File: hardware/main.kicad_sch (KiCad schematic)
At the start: 430 parts, among them J1 DS1128-09-S8B8X, J10 AS0BC21-S30BM-7H, J2 DS1128-09-S8B8X, J3 DS1128-09-S8B8X, J4 98424-G52-04ALF, J5 miniPCI-E_52P_5.2, J8 USB_C_Receptacle, J9 TYPE-C-31-M-12, Q1 SSM6J501NU, Q3 FDV301N, SW1 TS-1187A-B-A-B, SW2 TS-1187A-B-A-B, U1 SSD1306-OLED-0.91, U10 W25Q256FVEIG, U12 TPD2EUSB30, U13 TPD2EUSB30, U14 TPD2EUSB30, U15 IP5328P, U2 MT7621A, U3 TPS63020, U4 TPS63020, U5 MT3420B, U6 MT3420B, U7 MT3420B, U8 MT3420B, U9 NT5CB64M16FP-DH (!), Y1 X322540MPB4SI

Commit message: update pcb
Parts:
- removed C34: 100u, Capacitor_Tantalum_SMD:CP_EIA-7343-31_Kemet-D, symbol Device:C_Polarized_Small
- removed JP5, JP6: JP, MAS_Package_nostd:SolderJumper_Open_Pad0.5x0.8mm, symbol Jumper:Jumper_2_Open
- added C143, C34: 47u, Capacitor_SMD:C_0805_2012Metric, symbol Device:C_Small
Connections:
- net +1V0: now also C30.1, C41.1, C44.1, L5.2, R30.2; no longer C102.1, C104.1, C106.1, C109.1, C110.1, C115.1, C12.1, C135.1, C136.1, C8.1, C87.1, C93.1, L8.2, U2.N10 (DVDD_K_1), U2.N6 (AVDD10_AFE_P0), U2.N8 (AVDD10_AFE_P2), U2.P10 (DVDD_K_1), U2.P6 (AVDD10_AFE_P1), U2.P8 (AVDD10_AFE_P3), U2.R10 (DVDD_K_1), U2.R6 (AVDD10), U2.R8 (AVDD10_AFE_P4), U2.T10 (DVDD_K_1)
- net +1V2: now also C125.1, C51.1, C53.1, L6.2, R36.2
- net +5V: now also C143.1, C34.1
- net -BATT: now also C143.2, C34.2
- new net +1V0E: C102.1, C104.1, C106.1, C109.1, C110.1, C115.1, C12.1, C135.1, C136.1, C8.1, C87.1, C93.1, L8.2, U2.N10 (DVDD_K_1), U2.N6 (AVDD10_AFE_P0), U2.N8 (AVDD10_AFE_P2), U2.P10 (DVDD_K_1), U2.P6 (AVDD10_AFE_P1), U2.P8 (AVDD10_AFE_P3), U2.R10 (DVDD_K_1), U2.R6 (AVDD10), U2.R8 (AVDD10_AFE_P4), U2.T10 (DVDD_K_1)
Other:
- note added: "DDR3"
- note added: "Ethernet"
- note added: "Interface unit"
- note added: "M.2 connector"
- note added: "OLED"
- note added: "Power bank"
- note added: "Primary power"
- note added: "SPI Flash"
- note added: "SYS"
- note added: "Secondary power"
- note added: "USB3"
- note added: "mPCIe connector"
- moved on the sheet: C1, C10, C100, C101, C102, C103, C104, C105, C106, C107, C108, C109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

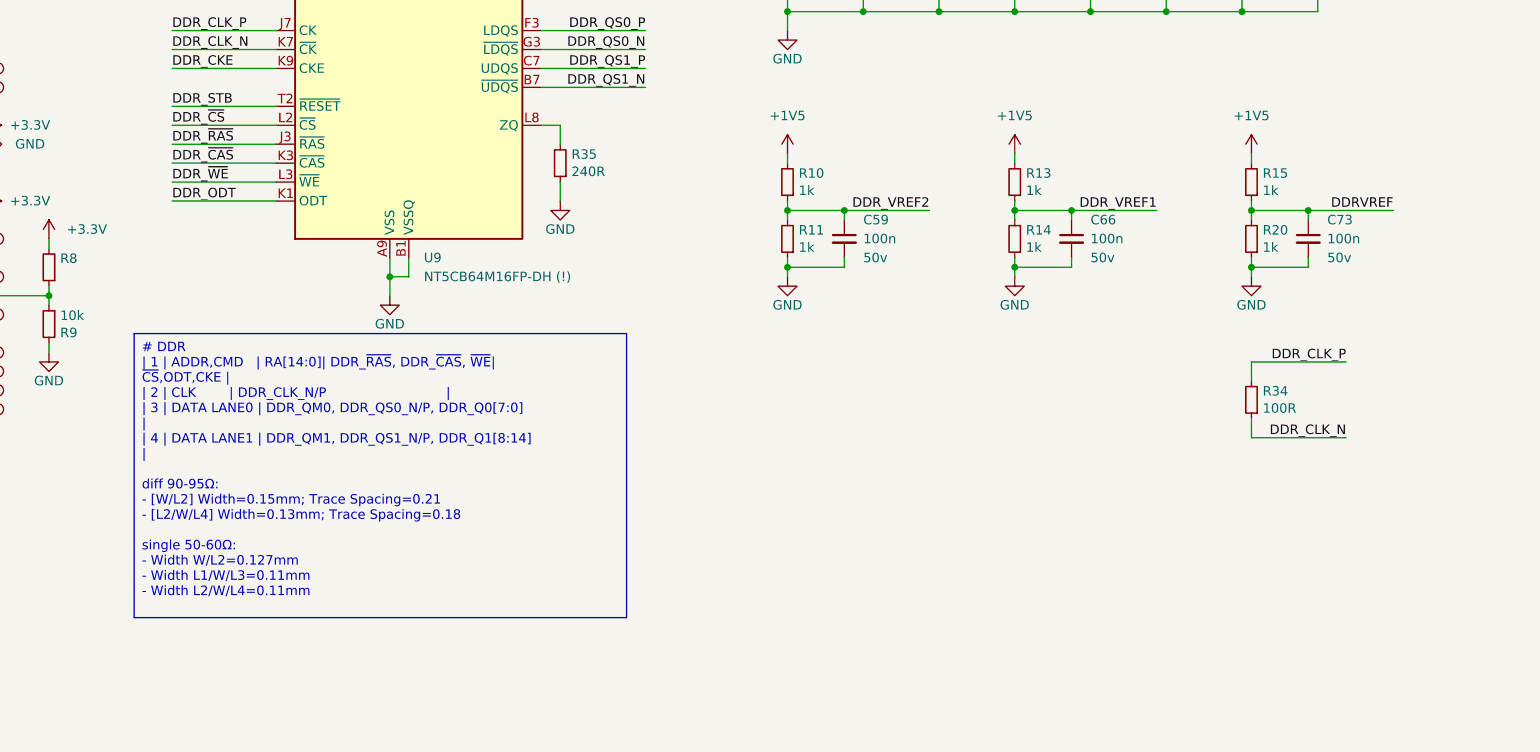
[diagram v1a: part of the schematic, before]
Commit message: custom layout ddr3
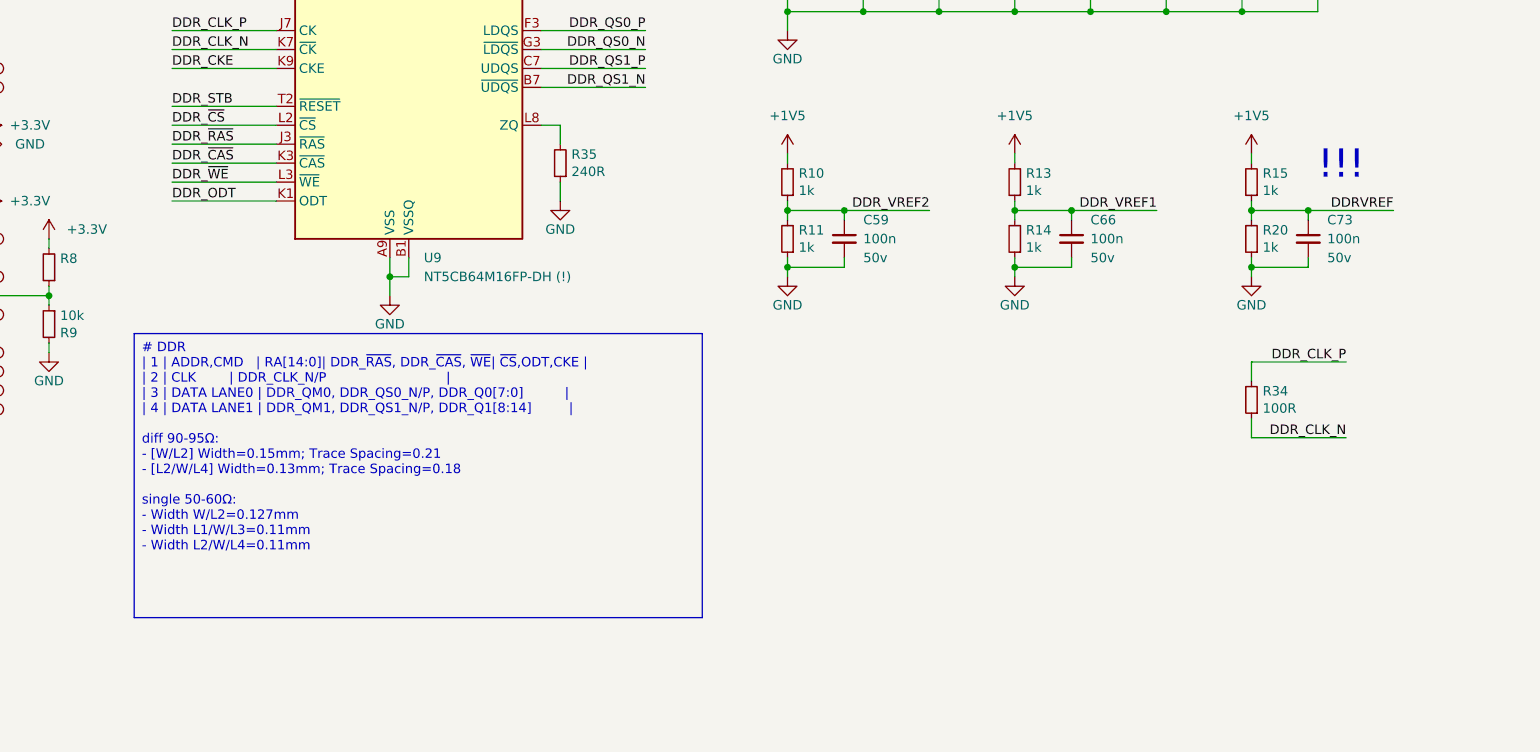
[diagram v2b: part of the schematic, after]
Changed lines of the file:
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@@
   )
   (text_box "# DDR\n| 1 | ADDR,CMD   | RA[14:0]| DDR_~{RAS}, DDR_~{CAS}, ~{WE}| ~{CS},ODT,CKE |\n| 2 | CLK        | DDR_CLK_N/P                             |\n| 3 | DATA LANE0 | DDR_QM0, DDR_QS0_N/P, DDR_Q0[7:0]          |\n| 4 | DATA LANE1 | DDR_QM1, DDR_QS1_N/P, DDR_Q1[8:14]         |\n\ndiff 90-95Ω:\n- [W/L2] Width=0.15mm; Trace Spacing=0.21\n- [L2/W/L4] Width=0.13mm; Trace Spacing=0.18\n\nsingle 50-60Ω:\n- Width W/L2=0.127mm\n- Width L1/W/L3=0.11mm\n- Width L2/W/L4=0.11mm"
-    (at 123.19 497.84 0) (size 66.04 38.1)
+    (at 123.19 497.84 0) (size 76.2 38.1)
     (stroke (width 0) (type default))
     (fill (type none))
@@
     (effects (font (size 3.81 3.81)) (justify left bottom))
   )
+  (text "!!!" (at 281.94 477.52 0)
+    (effects (font (size 3.81 3.81)) (justify left bottom))
+  )

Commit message: fixed ddr tracing, usb tracing
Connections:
- net USB_RXN: now also J8.B11 (RX1+); no longer J8.B10 (RX1-)
- net USB_RXP: now also J8.B10 (RX1-); no longer J8.B11 (RX1+)
- net _USB_TXN: now also J8.B2 (TX2+); no longer J8.B3 (TX2-)
- net _USB_TXP: now also J8.B3 (TX2-); no longer J8.B2 (TX2+)
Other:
- moved on the sheet: U12, U13, U14

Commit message: track tracing
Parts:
- added TP35, TP36, TP37: TP, MAS_Package_std:TestPoint_Pad_D1mm, symbol Connector:TestPoint
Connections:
- net +3V3: now also J7.4 (Pin_4); no longer J7.3 (Pin_3)
- net -BATT: now also C102.2, C104.2, C106.2, C109.2, C110.2, C134.2, C135.2, C136.2, C87.2, C93.2, J7.1 (Pin_1); no longer J7.4 (Pin_4)
- net G2-: no longer U2.Y17 (GE2_TXD3)
- net G3-: no longer U2.Y18 (GE2_TXD2)
- net G4-: no longer U2.W17 (GE2_TXD1)
- net JTCLK: now also J7.6 (Pin_6); no longer J7.1 (Pin_1)
- net JTMS: now also J7.7 (Pin_7); no longer J7.10 (Pin_10)
- net JTRST_N: now also J7.10 (Pin_10); no longer J7.7 (Pin_7)
- net PB_INT: now also U2.V18 (GE2_TXCLK); no longer U2.T18 (GE2_RXD1)
- net PWR5V_ON: now also U2.V16 (GE2_TXEN); no longer U2.U16 (GE2_RXD2)
- net PWR_ON: now also U2.W18 (GE2_TXD0); no longer U2.U17 (GE2_RXD3)
- net UART0_RXD: now also J7.5 (Pin_5); no longer J7.6 (Pin_6)
- net UART0_TXD: now also J7.3 (Pin_3); no longer J7.5 (Pin_5)
- net UART3_CTS: now also J10.34 (NC); no longer J10.36 (NC)
- net UART3_RTS: now also J10.36 (NC); no longer J10.30 (NC)
- net UART3_RXD: now also J10.32 (NC); no longer J10.34 (NC)
- net UART3_TXD: now also J10.30 (NC); no longer J10.32 (NC)
- net Y2-: now also U2.Y17 (GE2_TXD3); no longer U2.W18 (GE2_TXD0)
- net Y3-: now also U2.Y18 (GE2_TXD2); no longer U2.V16 (GE2_TXEN)
- net Y4-: now also U2.W17 (GE2_TXD1); no longer U2.V18 (GE2_TXCLK)
- new net: TP37.1, U2.T18 (GE2_RXD1)
- new net: TP36.1, U2.U16 (GE2_RXD2)
- new net: TP35.1, U2.U17 (GE2_RXD3)
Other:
- moved on the sheet: J7

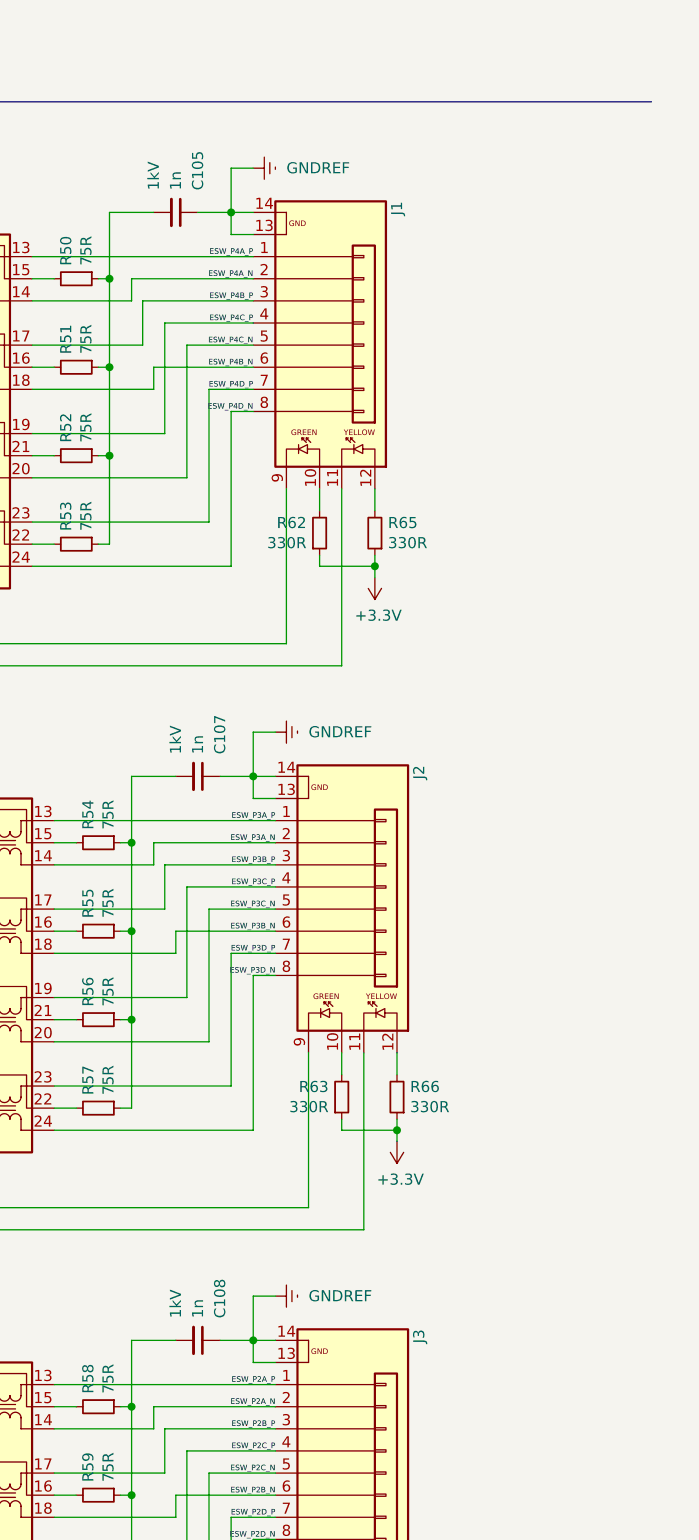
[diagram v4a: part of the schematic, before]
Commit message: impedance matching
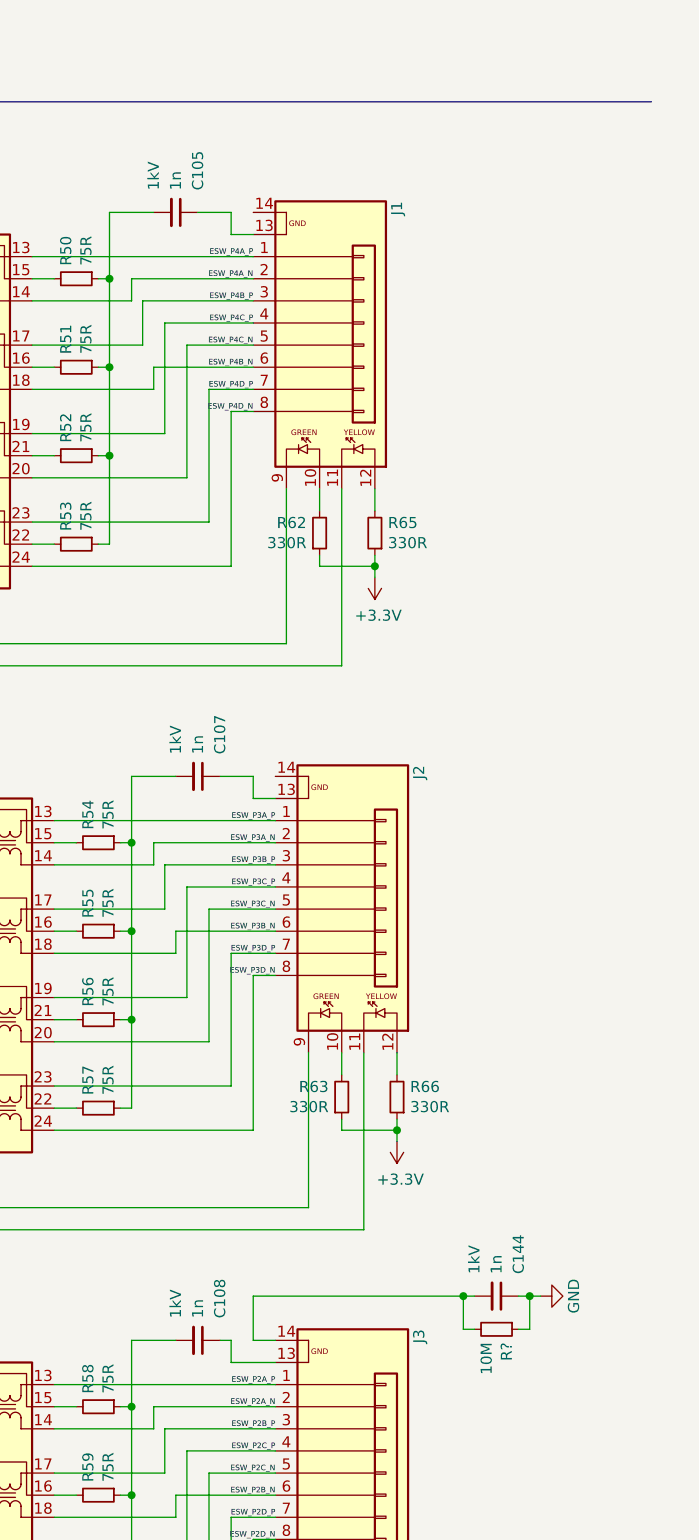
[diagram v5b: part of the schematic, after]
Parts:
- added C144: 1n, Capacitor_SMD:C_0805_2012Metric, symbol Device:C_Small
- added R?: 10M, Resistor_SMD:R_0805_2012Metric, symbol Device:R_Small
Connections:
- net -BATT: now also C144.1, R?.1
- removed net GNDREF: C105.1, C107.1, C108.1, J1.13, J1.14, J2.13, J2.14, J3.13, J3.14
- new net: C107.1, J2.13
- new net: C144.2, J3.14, R?.2
- new net: C108.1, J3.13
- new net: C105.1, J1.13

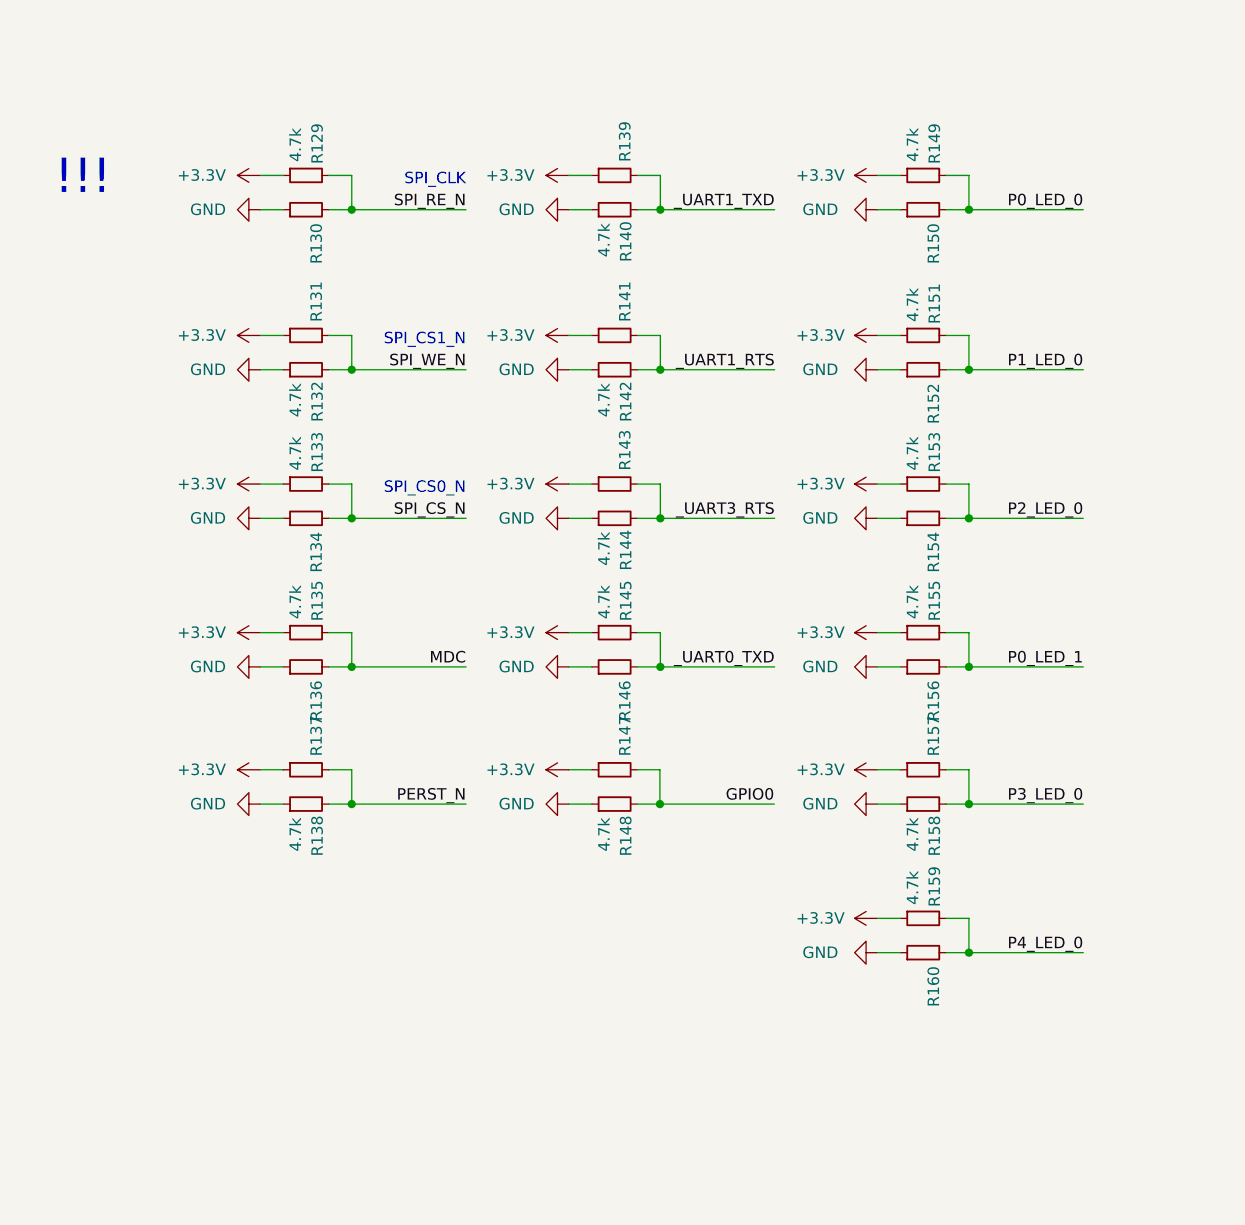
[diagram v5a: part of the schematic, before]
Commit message: update vias
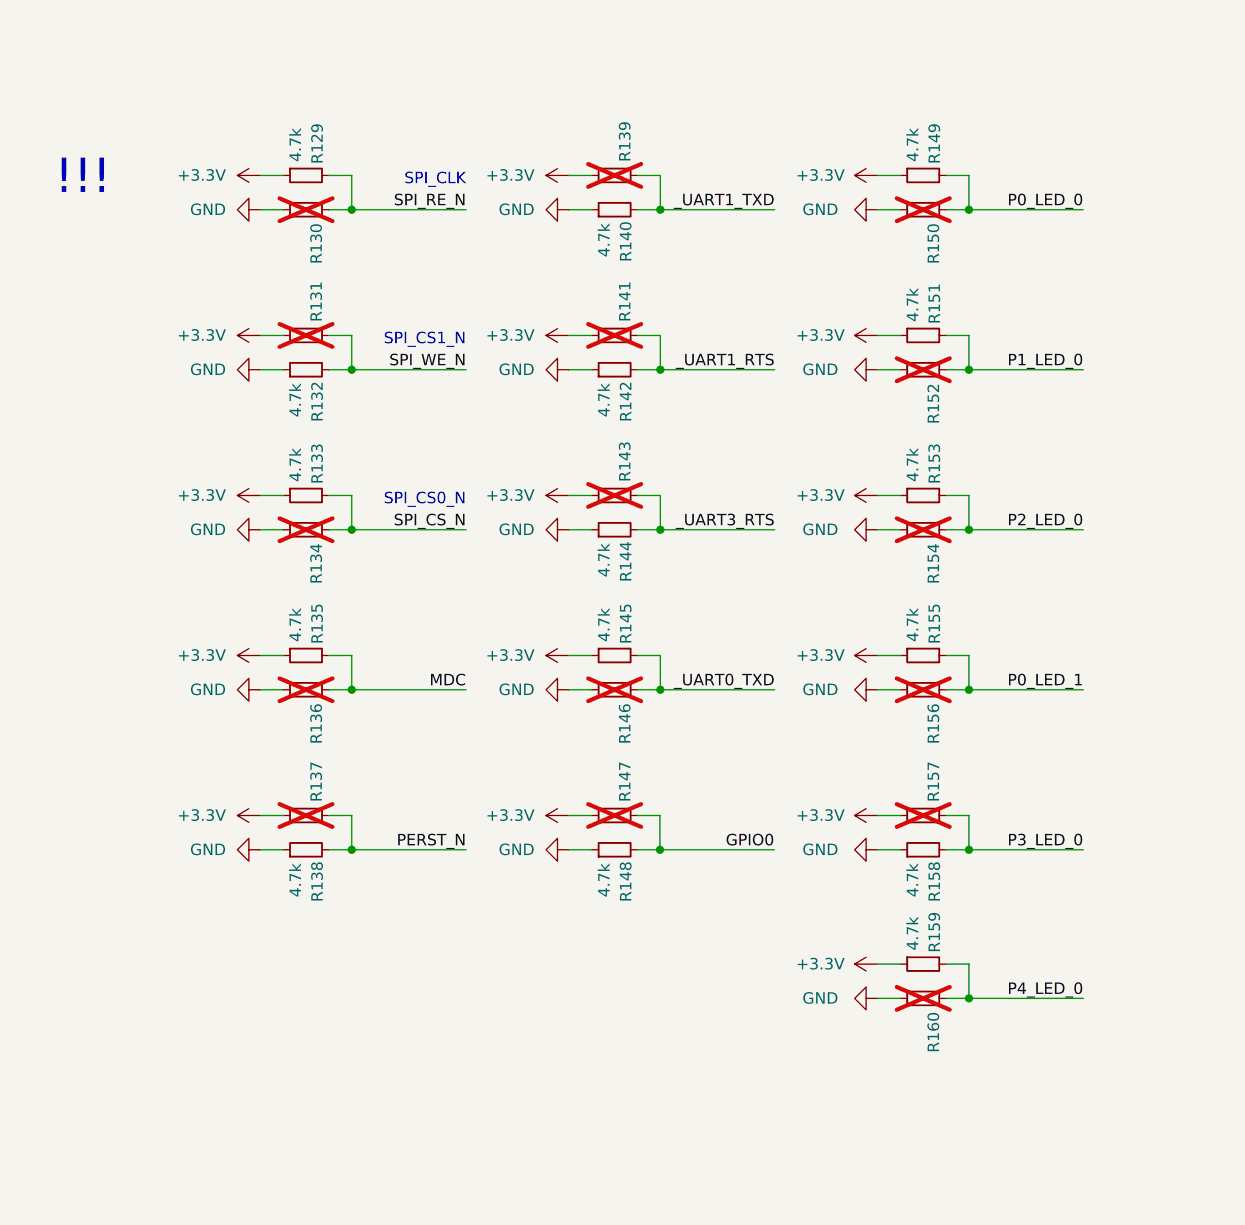
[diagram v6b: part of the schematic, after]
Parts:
- D1, D2: footprint Diode_SMD:D_0603_1608Metric -> LED_SMD:LED_0603_1608Metric
- R130, R131, R134, R136, R137, R139, R141, R143, R146, R147, R150, R152, R154, R156, R157, R160: now not fitted; now left out of the parts list
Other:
- moved on the sheet: R133, R135, R138, R144, R145, R148, R153, R155, R158, R159
